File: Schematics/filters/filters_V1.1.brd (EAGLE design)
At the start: 101 x 47.9 mm, 112 parts, among them IC1 NE5532N, IC2 NE5532N, IC3 NE5532N, IC4 NE5532N, IC5 NE5532N, IC6 NE5532N, IC7 NE5532N, J1 3_PIN_AMPCONN, J2 4_PIN_AMPCONN, J3 3_PIN_AMPCONN

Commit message: fixed the stupid mistake on the pot
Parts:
- C13, C14: value 47u -> 100u
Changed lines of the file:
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@@
 <attribute name="VALUE" x="45.847" y="33.8455" size="1.27" layer="27" ratio="10"/>
 </element>
-<element name="C13" library="rcl" package="C050-024X044" value="47u" x="14.605" y="30.7975" smashed="yes" rot="R90">
+<element name="C13" library="rcl" package="C050-024X044" value="100u" x="14.605" y="30.7975" smashed="yes" rot="R90">
 <attribute name="NAME" x="14.732" y="26.4795" size="0.889" layer="25" font="vector" ratio="15"/>
 <attribute name="VALUE" x="17.272" y="29.0195" size="1.27" layer="27" ratio="10" rot="R90"/>
 </element>
-<element name="C14" library="rcl" package="C050-024X044" value="47u" x="12.7" y="13.0175" smashed="yes" rot="R270">
+<element name="C14" library="rcl" package="C050-024X044" value="100u" x="12.7" y="13.0175" smashed="yes" rot="R270">
 <attribute name="NAME" x="10.287" y="14.478" size="0.889" layer="25" font="vector" ratio="15" rot="R270"/>
 <attribute name="VALUE" x="10.033" y="14.7955" size="1.27" layer="27" ratio="10" rot="R270"/>

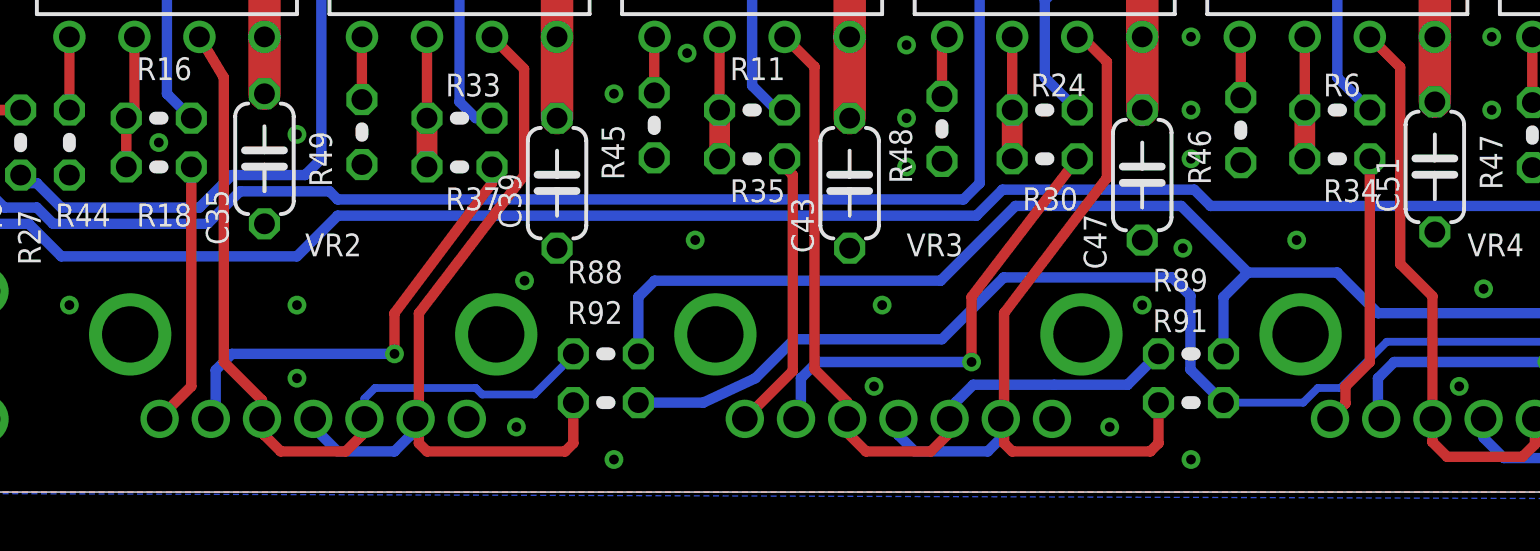
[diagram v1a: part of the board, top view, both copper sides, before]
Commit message: now all the filter board fixes are there
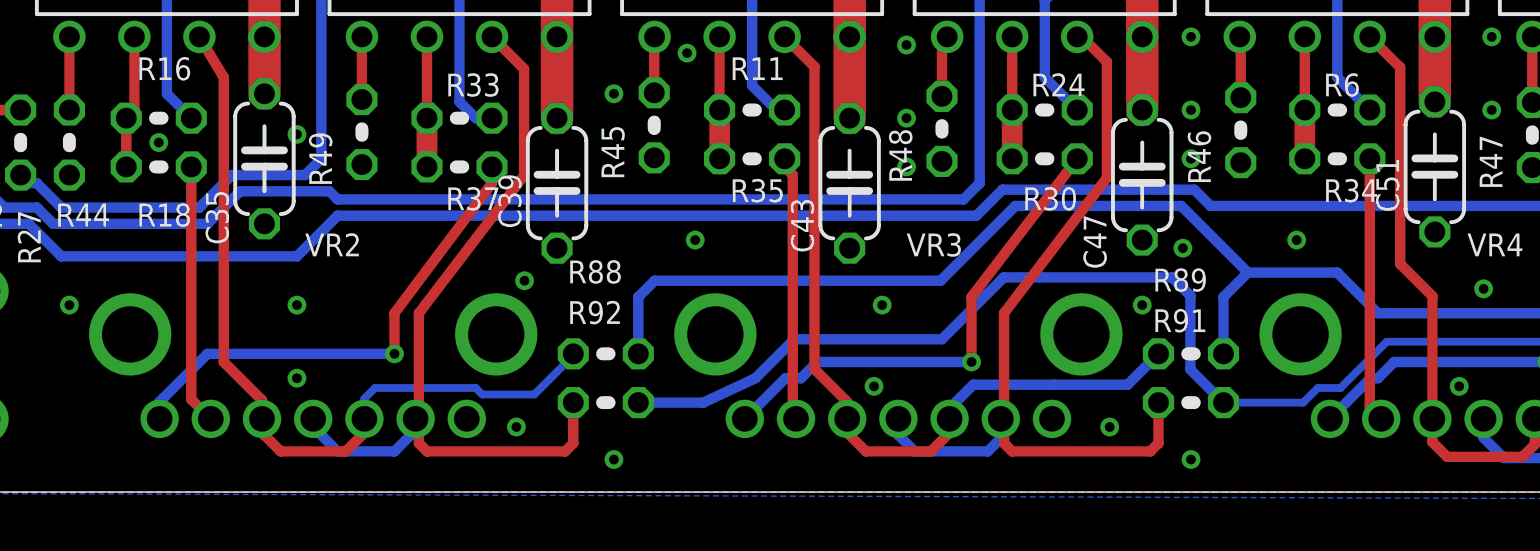
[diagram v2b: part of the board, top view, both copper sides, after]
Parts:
- R11, R16, R19, R24, R33, R6: value 10k -> 12k
- R12, R17, R21, R25, R36, R8: value 500 -> 1.2k
- R18, R29, R30, R34, R35, R37: value 2k -> 2.7k
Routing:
- net N$57: track 17.8 -> 19.2 mm
- net N$42: track 17.9 -> 19.1 mm
- net N$37: track 20.5 -> 21.4 mm
- net N$56: track 11.5 -> 10.8 mm

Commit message: Updated low pass filter amplifier with increased gain. Added filter response measurements
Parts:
- R21, R8: value 1.2k -> 3.9k
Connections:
- net GND: now also R47.1
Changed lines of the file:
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@@
 <attribute name="VALUE" x="82.7786" y="31.0261" size="1.27" layer="27" ratio="10" rot="R270"/>
 </element>
-<element name="R21" library="rcl" package="0204V" value="1.2k" x="87.63" y="28.8925" smashed="yes" rot="R270">
+<element name="R21" library="rcl" package="0204V" value="3.9k" x="87.63" y="28.8925" smashed="yes" rot="R270">
 <attribute name="NAME" x="88.0491" y="31.5214" size="0.889" layer="25" font="vector" ratio="15" rot="R90"/>
 <attribute name="VALUE" x="85.3186" y="31.0261" size="1.27" layer="27" ratio="10" rot="R270"/>
@@
 <attribute name="VALUE" x="71.3486" y="30.3911" size="1.27" layer="27" ratio="10" rot="R270"/>
 </element>
-<element name="R8" library="rcl" package="0204V" value="1.2k" x="76.2" y="28.2575" smashed="yes" rot="R270">
+<element name="R8" library="rcl" package="0204V" value="3.9k" x="76.2" y="28.2575" smashed="yes" rot="R270">
 <attribute name="NAME" x="75.7809" y="32.2961" size="0.889" layer="25" font="vector" ratio="15" rot="R270"/>
 <attribute name="VALUE" x="73.8886" y="30.3911" size="1.27" layer="27" ratio="10" rot="R270"/>
@@
 <contactref element="J2" pad="4"/>
 <via x="5.715" y="13.0175" extent="1-16" drill="0.381"/>
+<contactref element="R47" pad="1"/>
 </signal>
 <signal name="-12V">

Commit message: added names to input and output traces on filter board
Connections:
- net N$10 renamed RIGHT
- net N$108 renamed LEFT_IN
- net N$19 renamed BASS
- net N$26 renamed RIGHT_IN
- net N$38 renamed LEFT
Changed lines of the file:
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@@
 <?xml version="1.0" encoding="utf-8"?>
 <!DOCTYPE eagle SYSTEM "eagle.dtd">
-<eagle version="7.4.0">
+<eagle version="6.5.0">
 <drawing>
 <settings>
@@
 <pass name="Default">
 <param name="RoutingGrid" value="50mil"/>
-<param name="AutoGrid" value="1"/>
-<param name="Efforts" value="0"/>
-<param name="TopRouterVariant" value="1"/>
 <param name="tpViaShape" value="round"/>
-<param name="PrefDir.1" value="a"/>
+<param name="PrefDir.1" value="|"/>
 <param name="PrefDir.2" value="0"/>
 <param name="PrefDir.3" value="0"/>
@@
 <param name="PrefDir.14" value="0"/>
 <param name="PrefDir.15" value="0"/>
-<param name="PrefDir.16" value="a"/>
+<param name="PrefDir.16" value="-"/>
 <param name="cfVia" value="8"/>
 <param name="cfNonPref" value="5"/>
@@
 <wire x1="76.5175" y1="42.1875" x2="76.5575" y2="42.2275" width="0.4064" layer="1"/>
 </signal>
-<signal name="N$26">
+<signal name="RIGHT_IN">
 <contactref element="J1" pad="1"/>
 <contactref element="R1" pad="1"/>
@@
 <wire x1="10.4775" y1="33.02" x2="10.4775" y2="30.7975" width="0.4064" layer="1"/>
 </signal>
-<signal name="N$108">
+<signal name="LEFT_IN">
 <contactref element="J1" pad="2"/>
 <contactref element="R2" pad="1"/>
@@
 <wire x1="5.715" y1="32.385" x2="5.715" y2="30.48" width="0.4064" layer="1"/>
 </signal>
-<signal name="N$10">
+<signal name="RIGHT">
 <contactref element="R89" pad="2"/>
 <contactref element="R88" pad="2"/>
@@
 <wire x1="95.885" y1="8.255" x2="95.5675" y2="7.9375" width="0.4064" layer="1"/>
 </signal>
-<signal name="N$38">
+<signal name="LEFT">
 <contactref element="R91" pad="2"/>
 <contactref element="R92" pad="2"/>
@@
 <wire x1="36.83" y1="17.78" x2="36.83" y2="12.7" width="0.4064" layer="1"/>
 </signal>
-<signal name="N$19">
+<signal name="BASS">
 <contactref element="R90" pad="2"/>
 <contactref element="R41" pad="2"/>

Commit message: added folder for my case
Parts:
- removed C29, C31, C33, C35, C37, C39, C41, C43, C45, C47, C49, C51, C53, C55: 0.1uF, rcl:C050-024X044
- removed C36, C38: 100uF, rcl:E2,5-6
- removed J3: 3_PIN_AMPCONN, Amplifier_Parts:3_PIN_AMPCONN
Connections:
- removed net +12V: C31.2, C35.2, C36.+, C39.2, C43.2, C47.2, C51.2, C55.2, IC1.8, IC2.8, IC3.8, IC4.8, IC5.8, IC6.8, IC7.8, J3.2
- removed net -12V: C29.1, C33.1, C37.1, C38.-, C41.1, C45.1, C49.1, C53.1, IC1.4, IC2.4, IC3.4, IC4.4, IC5.4, IC6.4, IC7.4, J3.1
- new net V+: IC1.8, IC2.8, IC3.8, IC4.8, IC5.8, IC6.8, IC7.8
- new net V-: IC1.4, IC2.4, IC3.4, IC4.4, IC5.4, IC6.4, IC7.4
- net GND: no longer C29.2, C31.1, C33.2, C35.1, C36.-, C37.2, C38.+, C39.1, C41.2, C43.1, C45.2, C47.1, C49.2, C51.1, C53.2, C55.1, J3.3, VR2.P$3, VR2.P$4, VR3.P$3, VR3.P$4, VR4.P$3, VR4.P$4
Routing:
- net +12V: track 125.2 -> 0.00 mm
- net -12V: track 119.4 -> 0.00 mm
